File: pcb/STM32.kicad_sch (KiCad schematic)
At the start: 4 parts, among them CN1 Conn_02x08_Odd_Even, CN2 Conn_02x15_Odd_Even, CN3 Conn_02x10_Odd_Even, CN4 Conn_02x17_Odd_Even

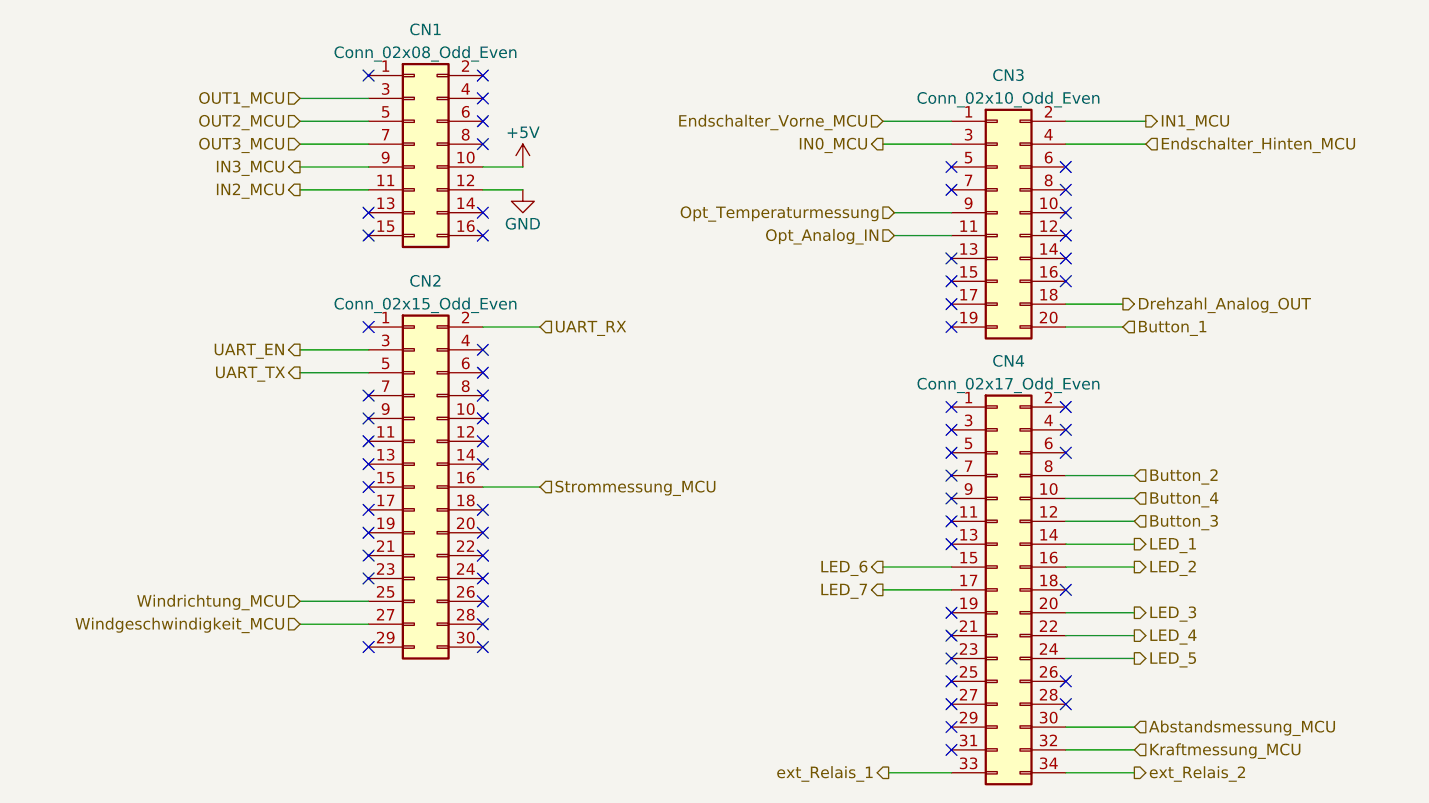
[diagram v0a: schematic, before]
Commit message: updated pcb and assigned correct pins
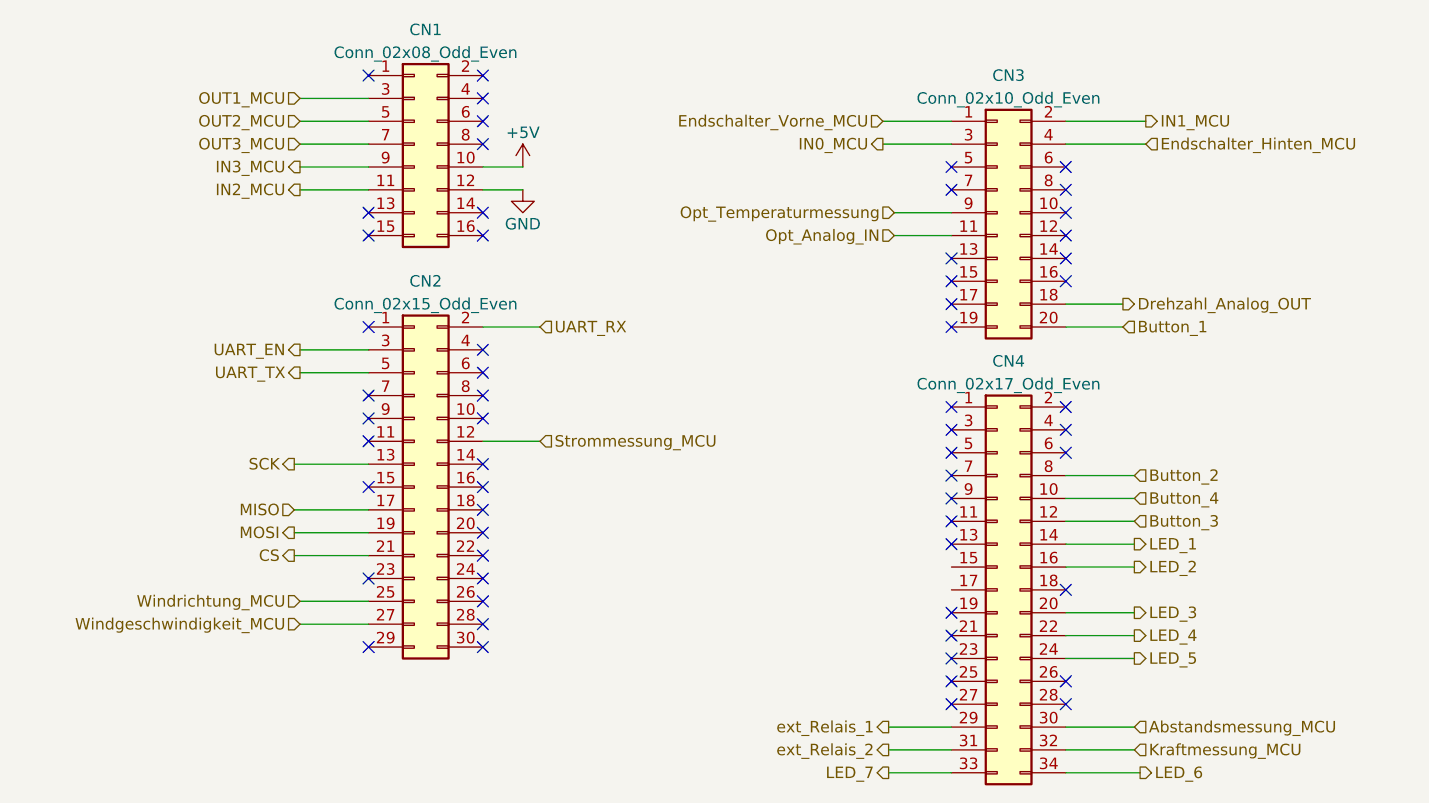
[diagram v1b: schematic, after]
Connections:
- net LED_6: now also CN4.34 (Pin_34); no longer CN4.15 (Pin_15)
- net LED_7: now also CN4.33 (Pin_33); no longer CN4.17 (Pin_17)
- net Strommessung_MCU: now also CN2.12 (Pin_12); no longer CN2.16 (Pin_16)
- net ext_Relais_1: now also CN4.29 (Pin_29); no longer CN4.33 (Pin_33)
- net ext_Relais_2: now also CN4.31 (Pin_31); no longer CN4.34 (Pin_34)
- net SCK: now reaches CN2.13 (Pin_13)
- net MISO: now reaches CN2.17 (Pin_17)
- net MOSI: now reaches CN2.19 (Pin_19)
- net CS: now reaches CN2.21 (Pin_21)
- no-connect marks 65 -> 59
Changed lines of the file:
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@@
   (no_connect (at 161.29 102.87))
   (no_connect (at 161.29 82.55))
-  (no_connect (at 96.52 93.98))
-  (no_connect (at 161.29 115.57))
-  (no_connect (at 96.52 96.52))
+  (no_connect (at 109.22 88.9))
   (no_connect (at 109.22 86.36))
-  (no_connect (at 173.99 110.49))
   (no_connect (at 96.52 71.12))
   (no_connect (at 109.22 48.26))
@@
   (no_connect (at 109.22 106.68))
   (no_connect (at 161.29 90.17))
-  (no_connect (at 109.22 83.82))
+  (no_connect (at 96.52 88.9))
   (no_connect (at 96.52 43.18))
   (no_connect (at 161.29 71.12))
   (no_connect (at 161.29 53.34))
-  (no_connect (at 96.52 88.9))
   (no_connect (at 173.99 100.33))
   (no_connect (at 96.52 58.42))
+  (no_connect (at 173.99 113.03))
   (no_connect (at 109.22 45.72))
   (no_connect (at 161.29 68.58))
@@
   (no_connect (at 109.22 101.6))
   (no_connect (at 161.29 107.95))
-  (no_connect (at 96.52 91.44))
   (no_connect (at 161.29 87.63))
   (no_connect (at 161.29 110.49))
+  (no_connect (at 173.99 110.49))
   (no_connect (at 173.99 55.88))
   (no_connect (at 109.22 93.98))
@@
   (no_connect (at 173.99 82.55))
   (no_connect (at 109.22 43.18))
-  (no_connect (at 96.52 86.36))
   (no_connect (at 173.99 58.42))
   (no_connect (at 109.22 96.52))
@@
   (no_connect (at 109.22 73.66))
   (no_connect (at 173.99 60.96))
-  (no_connect (at 173.99 113.03))
   (no_connect (at 109.22 50.8))
   (no_connect (at 109.22 58.42))
   (no_connect (at 109.22 60.96))
-  (no_connect (at 161.29 118.11))
   (no_connect (at 96.52 81.28))
   (no_connect (at 161.29 113.03))
@@
   (no_connect (at 96.52 106.68))
   (no_connect (at 173.99 53.34))
+  (wire (pts (xy 88.265 96.52) (xy 96.52 96.52))
+    (stroke (width 0) (type default))
+  )
+  (wire (pts (xy 154.305 120.65) (xy 161.29 120.65))
+    (stroke (width 0) (type default))
+  )
   (wire (pts (xy 173.99 102.87) (xy 181.61 102.87))
     (stroke (width 0) (type default))
@@
     (stroke (width 0) (type default))
   )
-  (wire (pts (xy 154.305 120.65) (xy 161.29 120.65))
+  (wire (pts (xy 173.99 120.65) (xy 182.245 120.65))
     (stroke (width 0) (type default))
   )
@@
     (stroke (width 0) (type default))
   )
+  (wire (pts (xy 88.265 93.98) (xy 96.52 93.98))
+    (stroke (width 0) (type default))
+  )
   (wire (pts (xy 88.9 55.88) (xy 96.52 55.88))
     (stroke (width 0) (type default))
@@
     (stroke (width 0) (type default))
   )
-  (wire (pts (xy 109.22 88.9) (xy 115.57 88.9))
+  (wire (pts (xy 109.22 83.82) (xy 115.57 83.82))
     (stroke (width 0) (type default))
   )
@@
     (stroke (width 0) (type default))
   )
+  (wire (pts (xy 154.305 115.57) (xy 161.29 115.57))
+    (stroke (width 0) (type default))
+  )
   (wire (pts (xy 88.9 101.6) (xy 96.52 101.6))
     (stroke (width 0) (type default))
@@
     (stroke (width 0) (type default))
   )
+  (wire (pts (xy 154.305 118.11) (xy 161.29 118.11))
+    (stroke (width 0) (type default))
+  )
   (wire (pts (xy 173.99 87.63) (xy 181.61 87.63))
     (stroke (width 0) (type default))
@@
     (stroke (width 0) (type default))
   )
-  (wire (pts (xy 153.67 100.33) (xy 161.29 100.33))
-    (stroke (width 0) (type default))
-  )
   (wire (pts (xy 88.9 104.14) (xy 96.52 104.14))
     (stroke (width 0) (type default))
@@
     (stroke (width 0) (type default))
   )
-  (wire (pts (xy 153.67 97.79) (xy 161.29 97.79))
+  (wire (pts (xy 88.265 91.44) (xy 96.52 91.44))
     (stroke (width 0) (type default))
   )
@@
     (stroke (width 0) (type default))
   )
-  (wire (pts (xy 173.99 120.65) (xy 181.61 120.65))
+  (wire (pts (xy 88.265 86.36) (xy 96.52 86.36))
     (stroke (width 0) (type default))
   )
@@
     (stroke (width 0) (type default))
   )
+  (hierarchical_label "MOSI" (shape output) (at 88.265 93.98 180) (fields_autoplaced)
+    (effects (font (size 1.27 1.27)) (justify right))
+  )
   (hierarchical_label "Button_1" (shape input) (at 180.34 71.12 0) (fields_autoplaced)
     (effects (font (size 1.27 1.27)) (justify left))
@@
     (effects (font (size 1.27 1.27)) (justify right))
   )
+  (hierarchical_label "CS" (shape output) (at 88.265 96.52 180) (fields_autoplaced)
+    (effects (font (size 1.27 1.27)) (justify right))
+  )
   (hierarchical_label "UART_EN" (shape output) (at 88.9 73.66 180) (fields_autoplaced)
     (effects (font (size 1.27 1.27)) (justify right))
@@
     (effects (font (size 1.27 1.27)) (justify left))
   )
-  (hierarchical_label "LED_6" (shape output) (at 153.67 97.79 180) (fields_autoplaced)
+  (hierarchical_label "LED_6" (shape output) (at 182.245 120.65 0) (fields_autoplaced)
+    (effects (font (size 1.27 1.27)) (justify left))
+  )
+  (hierarchical_label "MISO" (shape input) (at 88.265 91.44 180) (fields_autoplaced)
     (effects (font (size 1.27 1.27)) (justify right))
   )
@@
     (effects (font (size 1.27 1.27)) (justify right))
   )
+  (hierarchical_label "SCK" (shape output) (at 88.265 86.36 180) (fields_autoplaced)
+    (effects (font (size 1.27 1.27)) (justify right))
+  )
   (hierarchical_label "UART_RX" (shape input) (at 115.57 71.12 0) (fields_autoplaced)
     (effects (font (size 1.27 1.27)) (justify left))
   )
-  (hierarchical_label "ext_Relais_2" (shape output) (at 181.61 120.65 0) (fields_autoplaced)
-    (effects (font (size 1.27 1.27)) (justify left))
-  )
-  (hierarchical_label "LED_7" (shape output) (at 153.67 100.33 180) (fields_autoplaced)
+  (hierarchical_label "ext_Relais_2" (shape output) (at 154.305 118.11 180) (fields_autoplaced)
+    (effects (font (size 1.27 1.27)) (justify right))
+  )
+  (hierarchical_label "LED_7" (shape output) (at 154.305 120.65 180) (fields_autoplaced)
     (effects (font (size 1.27 1.27)) (justify right))
   )
@@
     (effects (font (size 1.27 1.27)) (justify right))
   )
-  (hierarchical_label "Strommessung_MCU" (shape input) (at 115.57 88.9 0) (fields_autoplaced)
+  (hierarchical_label "Strommessung_MCU" (shape input) (at 115.57 83.82 0) (fields_autoplaced)
     (effects (font (size 1.27 1.27)) (justify left))
   )
@@
     (effects (font (size 1.27 1.27)) (justify left))
   )
-  (hierarchical_label "ext_Relais_1" (shape output) (at 154.305 120.65 180) (fields_autoplaced)
-    (effects (font (size 1.27 1.27)) (justify right))
-  )
+  (hierarchical_label "ext_Relais_1" (shape output) (at 154.305 115.57 180) (fields_autoplaced)
+    (effects (font (size 1.27 1.27)) (justify right))
+  )

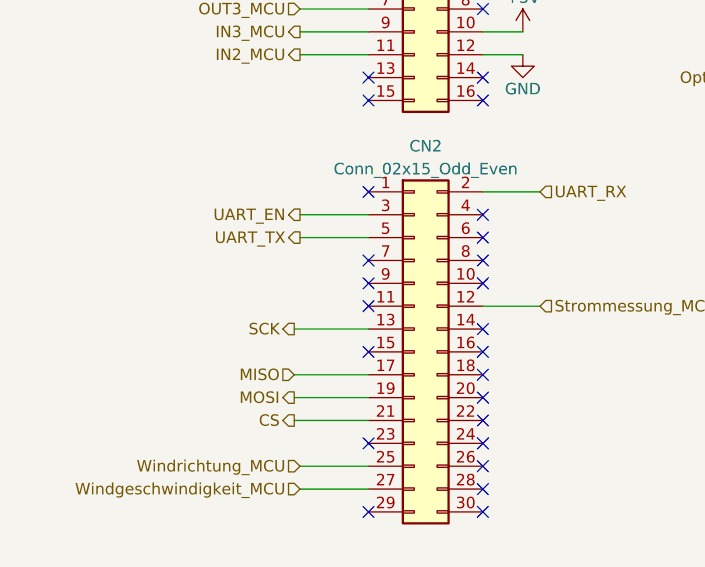
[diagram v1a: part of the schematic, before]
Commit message: finished assigning pins and creating pcb
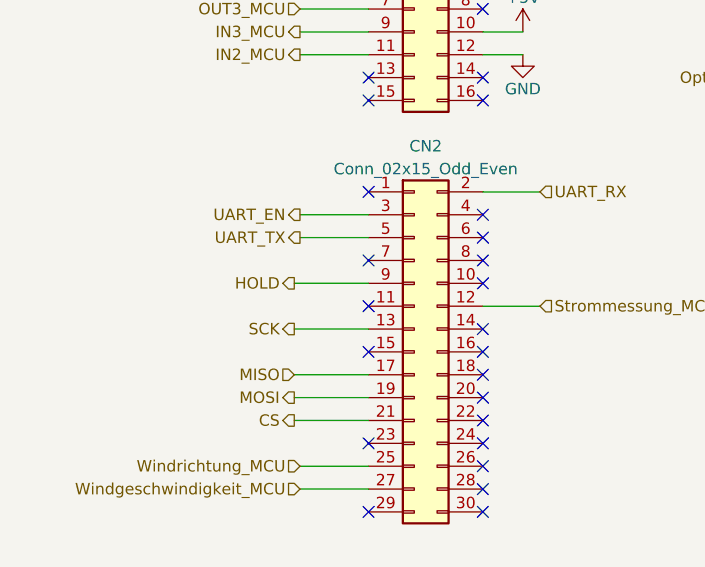
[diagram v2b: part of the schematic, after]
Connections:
- net HOLD: now reaches CN2.9 (Pin_9)
- no-connect marks 59 -> 58
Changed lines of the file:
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@@
   (no_connect (at 96.52 60.96))
   (no_connect (at 109.22 101.6))
+  (no_connect (at 96.52 99.06))
   (no_connect (at 161.29 107.95))
   (no_connect (at 161.29 87.63))
@@
   (no_connect (at 109.22 91.44))
   (no_connect (at 161.29 95.25))
-  (no_connect (at 96.52 99.06))
   (no_connect (at 109.22 104.14))
   (no_connect (at 161.29 66.04))
@@
   (no_connect (at 109.22 58.42))
   (no_connect (at 109.22 60.96))
-  (no_connect (at 96.52 81.28))
   (no_connect (at 161.29 113.03))
   (no_connect (at 161.29 105.41))
@@
     (stroke (width 0) (type default))
   )
+  (wire (pts (xy 88.265 81.28) (xy 96.52 81.28))
+    (stroke (width 0) (type default))
+  )
   (wire (pts (xy 173.99 102.87) (xy 181.61 102.87))
     (stroke (width 0) (type default))
@@
     (effects (font (size 1.27 1.27)) (justify left))
   )
+  (hierarchical_label "HOLD" (shape output) (at 88.265 81.28 180) (fields_autoplaced)
+    (effects (font (size 1.27 1.27)) (justify right))
+  )
   (hierarchical_label "IN3_MCU" (shape output) (at 88.9 53.34 180) (fields_autoplaced)
